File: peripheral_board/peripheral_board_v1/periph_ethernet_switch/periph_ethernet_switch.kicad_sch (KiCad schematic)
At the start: 52 parts, among them SW1 EVPAA602W, U1 KSZ9896CTXI, X1 XXCCCLNANF-25M

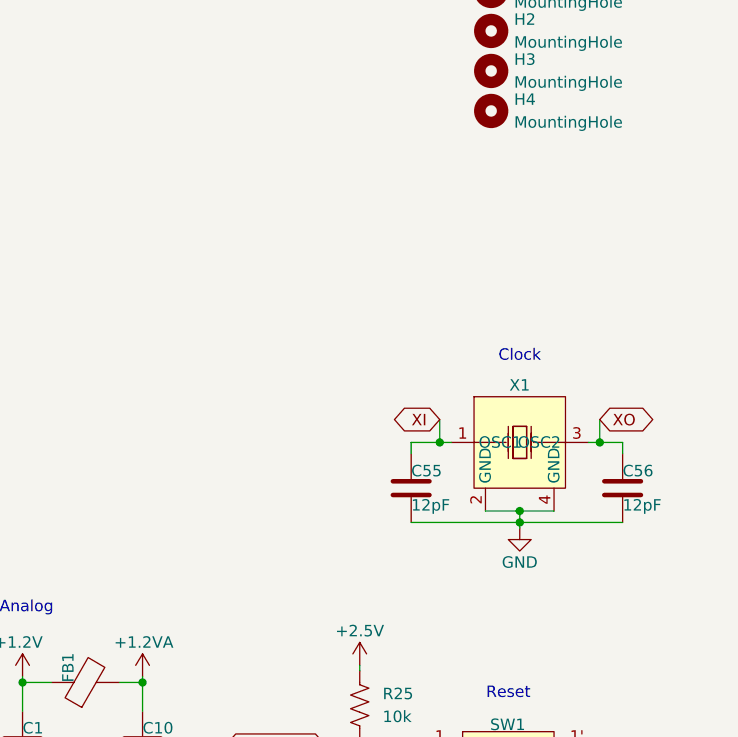
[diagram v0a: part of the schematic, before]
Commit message: Minor update to the schematic and board
Added a resistor to the clock and changed some of the trace connections
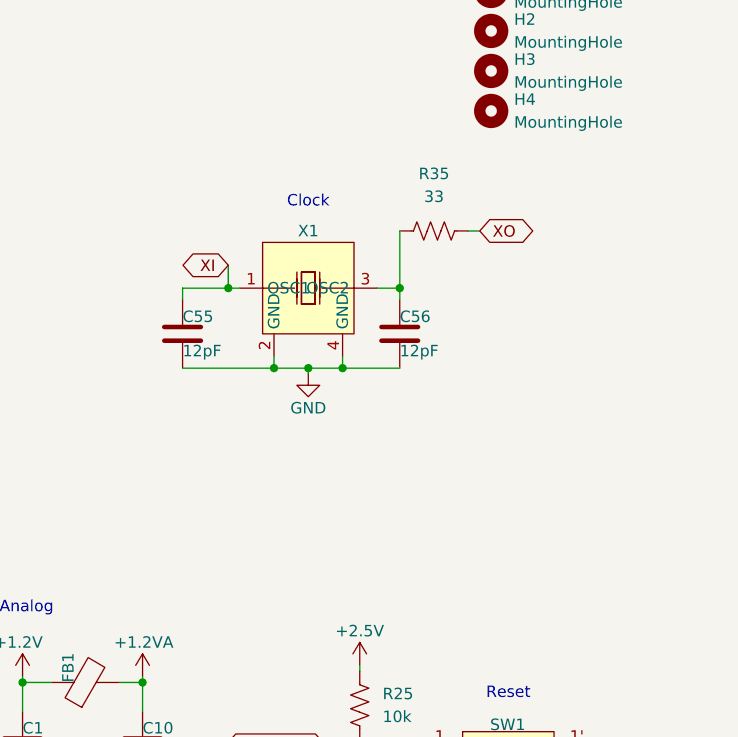
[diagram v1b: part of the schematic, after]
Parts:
- added R35: 33, Resistor_SMD:R_0603_1608Metric, symbol Device:R_US
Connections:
- net XO: now also R35.1; no longer C56.1, X1.3 (OSC2)
- new net: C56.1, R35.2, X1.3 (OSC2)
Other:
- moved on the sheet: C55, C56, X1

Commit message: Small changes from Microchip
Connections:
- net +1.2V: now also C15.1, C19.1, C22.1, U1.11 (DVDDL), U1.23 (DVDDL), U1.45 (DVDDL)
- net +1.2VA: no longer C15.1, C19.1, C22.1, U1.11 (AVDDL), U1.23 (AVDDL), U1.45 (AVDDL)
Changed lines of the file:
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@@
 			)
 		)
-		(property "Value" "+1.2VA"
+		(property "Value" "+1.2V"
 			(at 27.94 86.36 0)
 			(effects
@@
 			)
 		)
-		(property "Value" "+1.2VA"
+		(property "Value" "+1.2V"
 			(at 151.13 169.545 0)
 			(effects
@@
 			)
 		)
-		(property "Value" "+1.2VA"
+		(property "Value" "+1.2V"
 			(at 34.29 116.205 0)
 			(effects

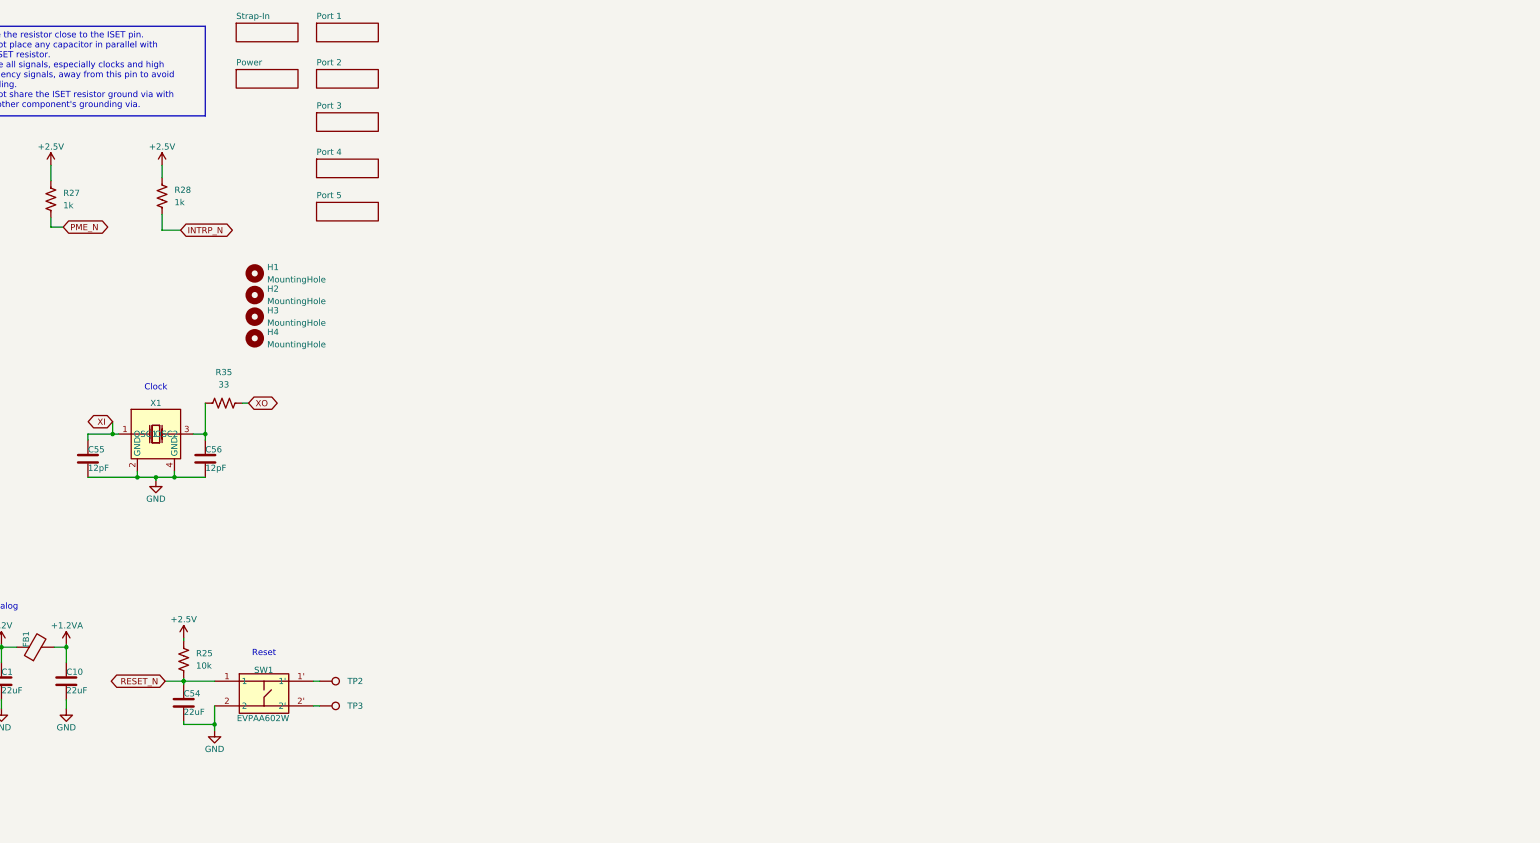
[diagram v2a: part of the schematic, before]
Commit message: WIP for new switch
Made some minor changes which are detailed in Notion.
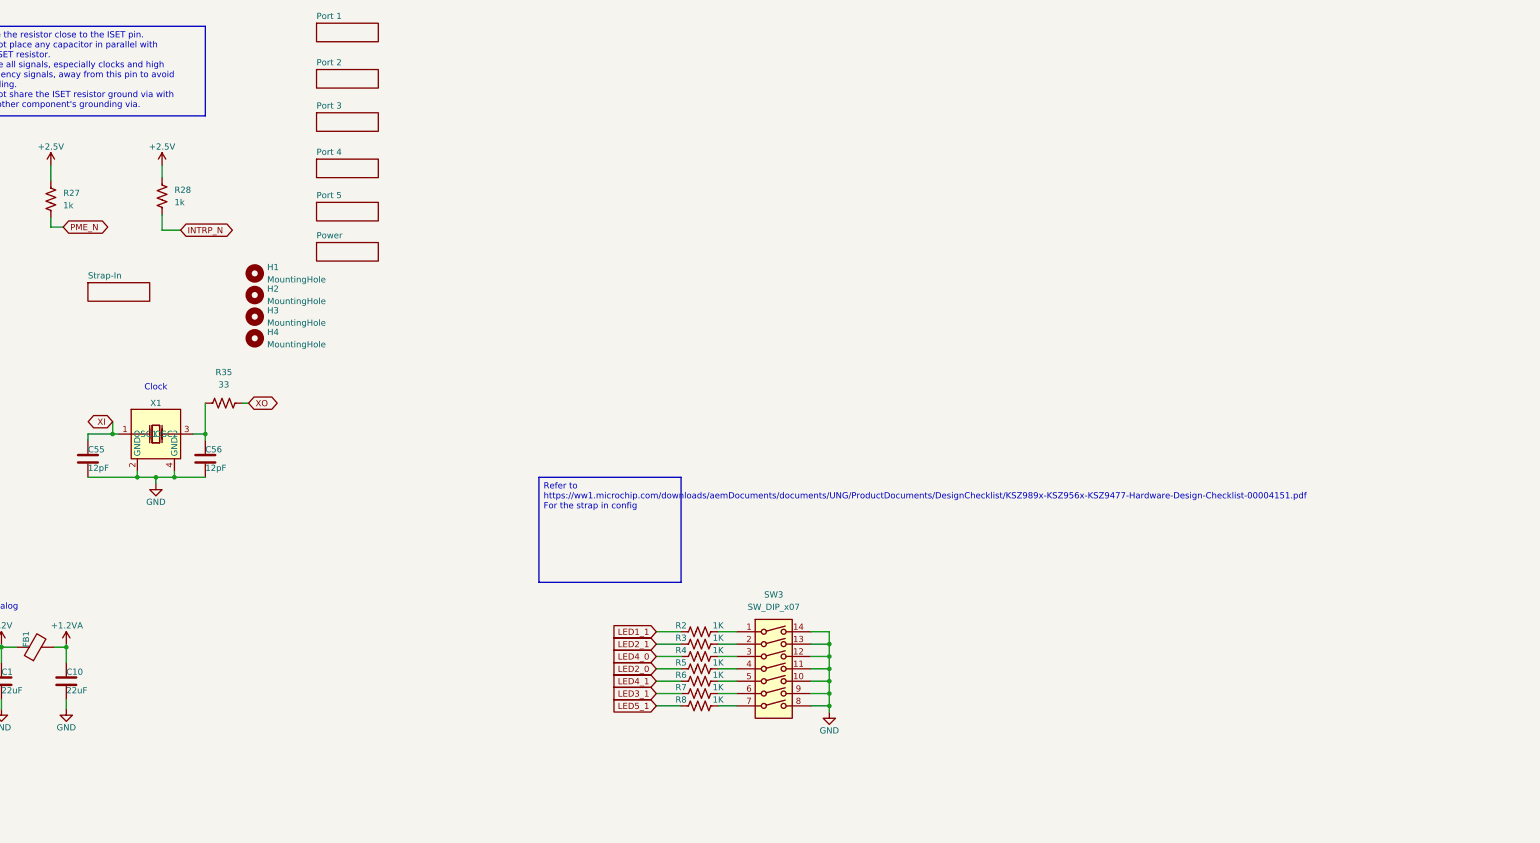
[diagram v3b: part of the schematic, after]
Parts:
- removed C54: 22uF, Capacitor_SMD:C_0603_1608Metric, symbol Device:C
- removed R25: 10k, Resistor_SMD:R_0603_1608Metric, symbol Device:R_US
- removed SW1: EVPAA602W, SCALES:KEY-TH_4P-L3.5-W4.9-P2.80-LS4.3, symbol easyeda2kicad:EVPAA602W
- removed TP2, TP3: TestPoint, TestPoint:TestPoint_Pad_1.0x1.0mm, symbol Connector:TestPoint
- added R2, R3, R4, R5, R6, R7, R8: 1K, Resistor_SMD:R_0603_1608Metric, symbol Device:R_US
- added SW3: SW_DIP_x07, symbol Switch:SW_DIP_x07
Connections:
- net GND: now also SW3.10, SW3.11, SW3.12, SW3.13, SW3.14, SW3.8, SW3.9
- net LED1_1: now also R2.2
- net LED2_0: now also R5.2
- net LED2_1: now also R3.2
- net LED3_1: now also R7.2
- net LED4_0: now also R4.2
- net LED4_1: now also R6.2
- net LED5_1: now also R8.2
- new net: R8.1, SW3.7
- new net: R4.1, SW3.3
- new net: R7.1, SW3.6
- new net: R2.1, SW3.1
- new net: R3.1, SW3.2
- new net: R5.1, SW3.4
- new net: R6.1, SW3.5
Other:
- note removed: "Reset"

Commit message: Changes to the board layout
Need to finish doing some layout but waiting on Microchip to confirm with what I have. Might want to change the EDA symbol for the switch IC.
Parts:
- SW1: renamed from SW3; footprint (none) -> Button_Switch_THT:SW_DIP_SPSTx07_Slide_6.7x19.34mm_W7.62mm_P2.54mm_LowProfile
- renumbered C4 to C1, C19 to C10, C27 to C11, C9 to C12, C11 to C13, C12 to C14, C26 to C15, C31 to C16, C6 to C17, C2 to C18, C29 to C19, C17 to C2, C21 to C20, C30 to C21, C53 to C22, C22 to C23, C23 to C24, C24 to C25, C25 to C26, C3 to C27, C52 to C28, C5 to C29, C14 to C3, C28 to C30, C20 to C31, C1 to C32, C10 to C33, C55 to C34, C56 to C35, C7 to C4, C18 to C5, C15 to C6, C8 to C7, C13 to C8, C16 to C9, FB2 to FB1, FB1 to FB2, R26 to R1, R8 to R10, R35 to R11, R27 to R2, R28 to R3, R2 to R4, R3 to R5, R4 to R6, R5 to R7, R6 to R8, R7 to R9
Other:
- moved on the sheet: R10, R4, R5, R6, R7, R8, R9, SW1

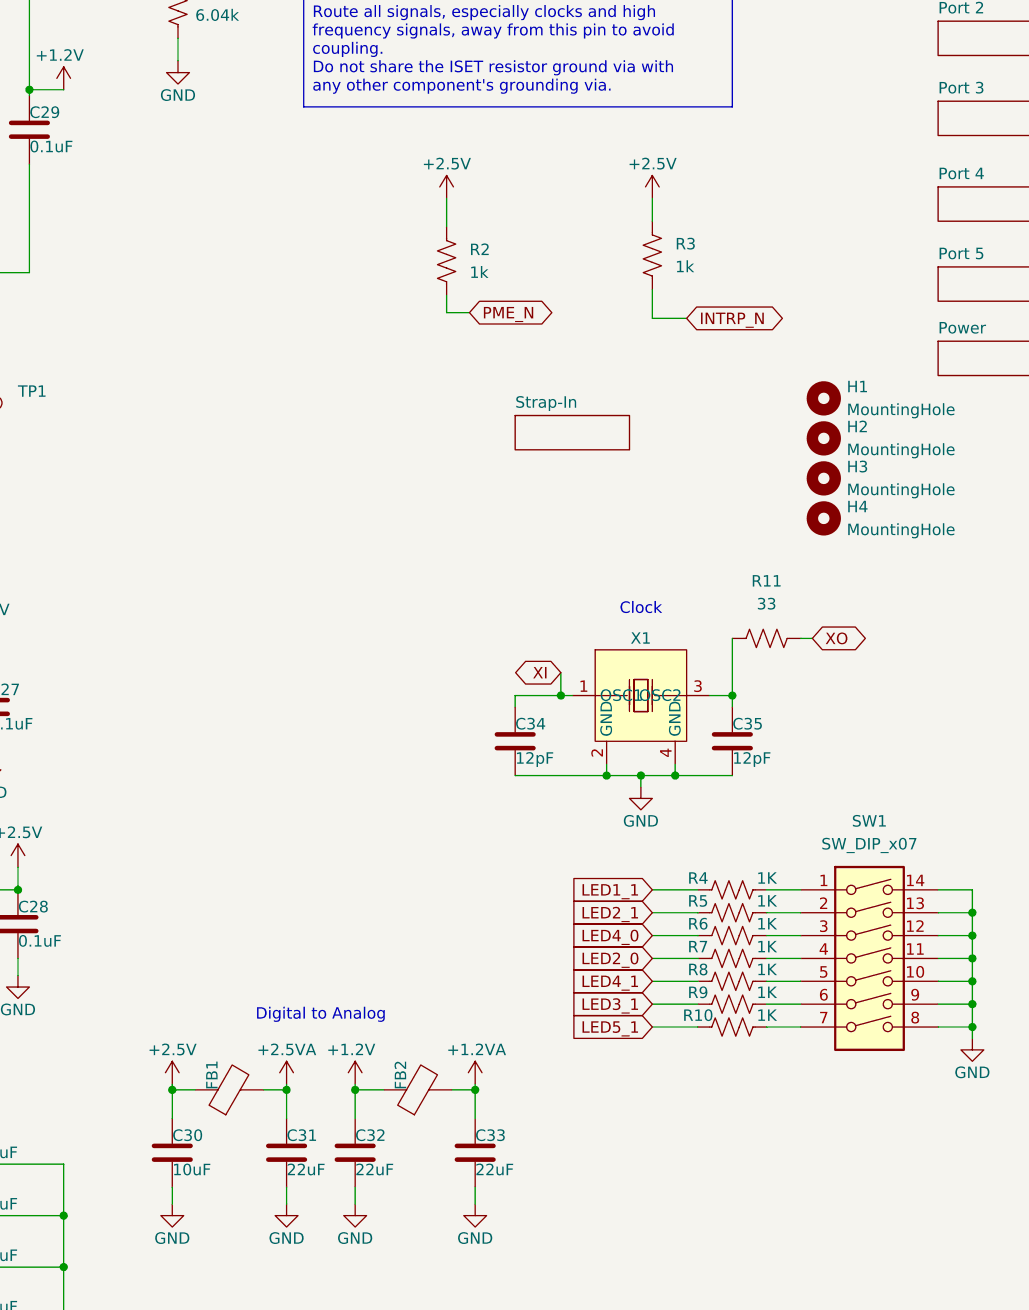
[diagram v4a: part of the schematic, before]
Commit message: Changes based on Microchip support
Made some changes for the strap in configuration. Did some some layout changes. Used the same circuit for the clock and strap in switch from their other Dev kit. Waiting on them to get back to me for a potential schematic review/board review.
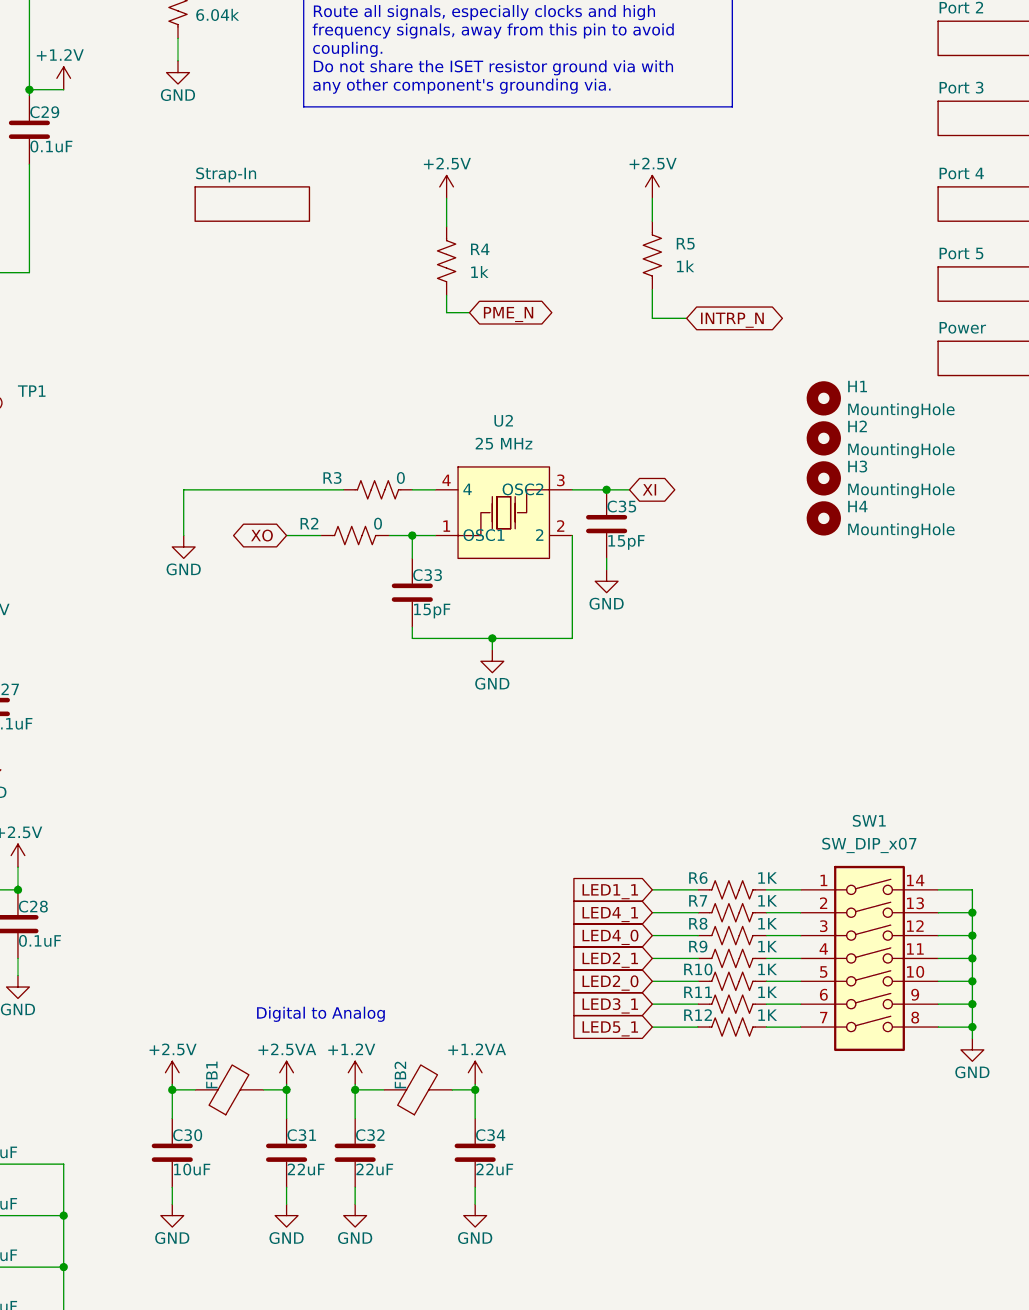
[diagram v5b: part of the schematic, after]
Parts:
- removed C34: 12pF, Capacitor_SMD:C_0603_1608Metric, symbol Device:C
- removed R11: 33, Resistor_SMD:R_0603_1608Metric, symbol Device:R_US
- removed X1: XXCCCLNANF-25M, SCALES:CRYSTAL-SMD_4P-L3.2-W2.5-BL, symbol SCALES:XXCCCLNANF-25M
- added C33: 15pF, Capacitor_SMD:C_0603_1608Metric, symbol Device:C
- added R2, R3: 0, Resistor_SMD:R_0603_1608Metric, symbol Device:R_US
- added U2: 25 MHz, SCALES:CRYSTAL-SMD_4P-L3.2-W2.5-TR, symbol SCALES:ABM8G-25.000MHZ-B4Y-T
- C35: value 12pF -> 15pF
- renumbered C33 to C34, R8 to R10, R9 to R11, R10 to R12, R2 to R4, R3 to R5, R4 to R6, R5 to R7, R6 to R8, R7 to R9
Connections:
- net GND: now also C33.2, R3.2, U2.2
- net LED2_0: now also R10.2; no longer R9.2
- net LED2_1: now also R9.2; no longer R7.2
- net LED4_1: now also R7.2; no longer R10.2
- net XI: now also C35.1, U2.3 (OSC2)
- net XO: now also R2.2
- new net: C33.1, R2.1, U2.1 (OSC1)
- new net: R3.1, U2.4
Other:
- note removed: "Clock"
